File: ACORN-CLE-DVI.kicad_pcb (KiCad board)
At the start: 4 copper layers, 28.1 x 19.9 mm, 26 parts, among them J1 HDMI_A, J2 Acorn, U1 PI3HDX511D, U2 XC9141

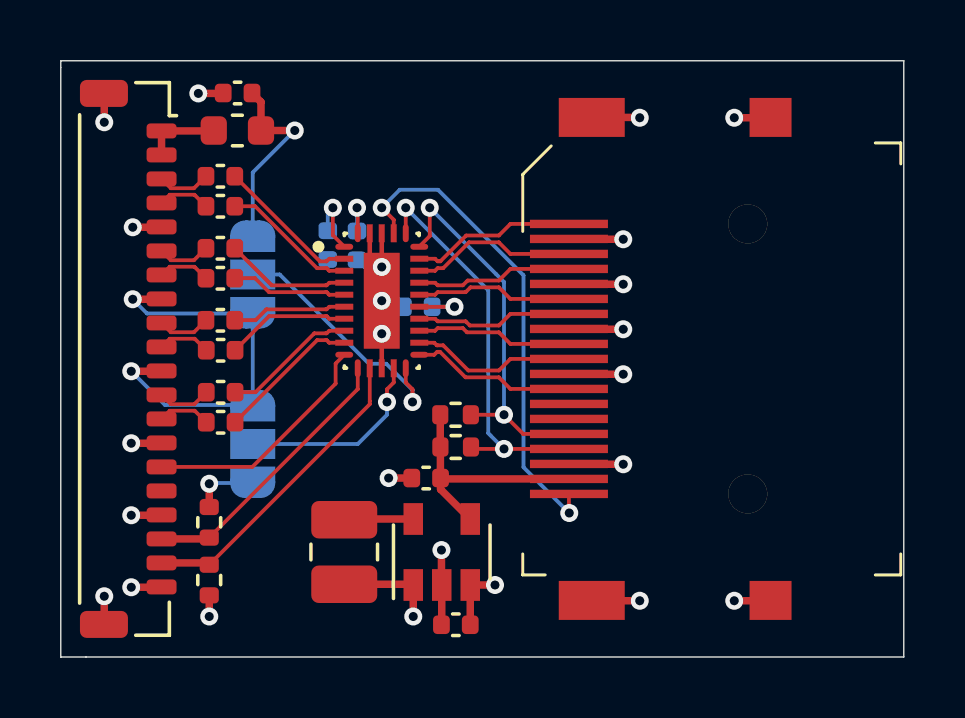
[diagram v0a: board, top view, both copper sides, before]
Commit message: move all capacitors to top layer
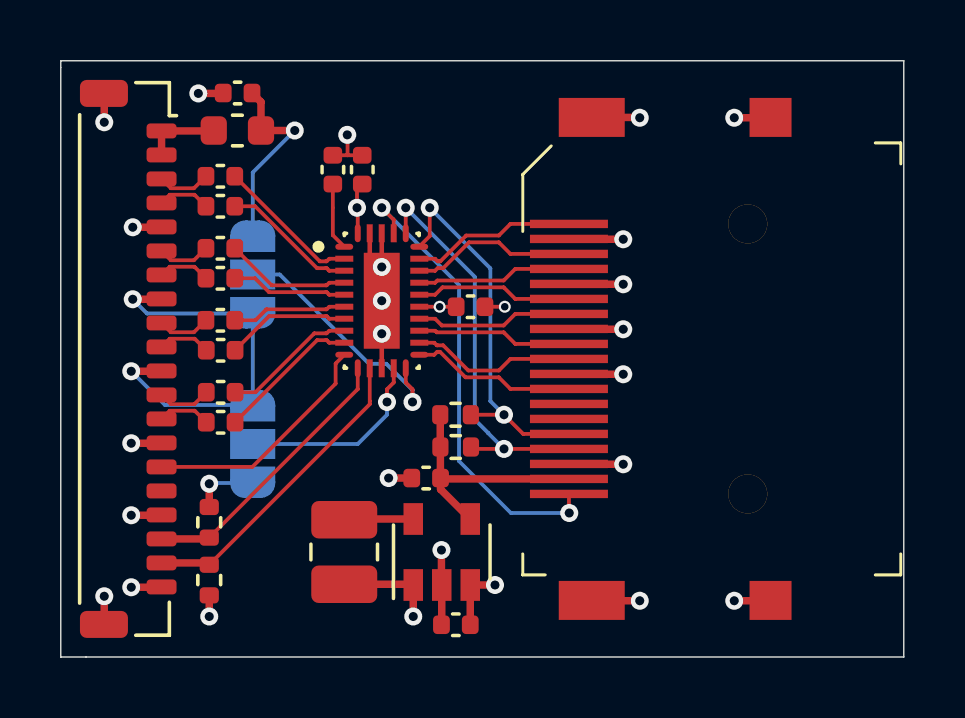
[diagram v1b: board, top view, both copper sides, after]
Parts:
- C10, C14, C9: moved to F.Cu
- moved C9 2.53 mm to (149.8, 97.1), turned to 90 degrees
- moved C14 2.52 mm to (148.8, 97.1), turned to 90 degrees
- moved C10 1.76 mm to (153.4, 101.7), turned to 0 degrees
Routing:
- net /HPD_SINK: track 16.3 -> 15.5 mm
- net +3V3: track 18.4 -> 17.9 mm
- net GND: track 48.3 -> 47.9 mm, vias 23 -> 25
- net Net-(C14-Pad1): track 2.29 -> 2.25 mm, vias 1 -> 0
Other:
- board text added: "DVI Adapter and Redriver v1.1"
- board text removed: "DVI Adapter and Redriver v1.0"
